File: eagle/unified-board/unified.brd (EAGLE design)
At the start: 203.2 x 101.6 mm, 299 parts, among them IC101 THAT151x, IC201 THAT151x, IC301 THAT151x, IC401 THAT151x, J103 phantom, J104 eqout, J105 eqout, J203 phantom, J204 eqout, J205 eqout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

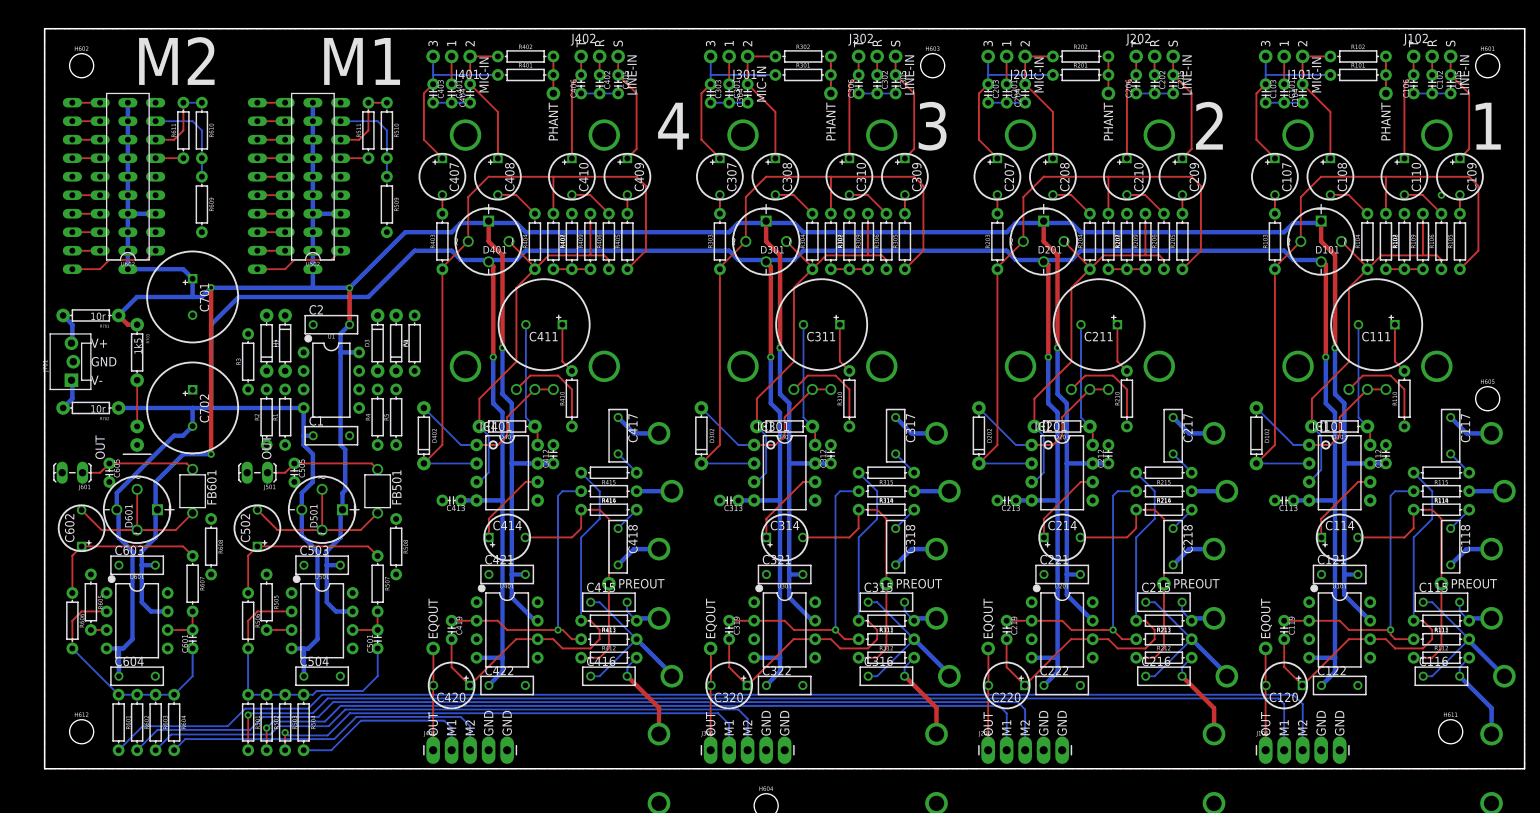
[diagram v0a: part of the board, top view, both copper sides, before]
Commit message: Possibly complete?
doublechecked all IC footprints.
Routed the peak detector & found 1uf caps for it.
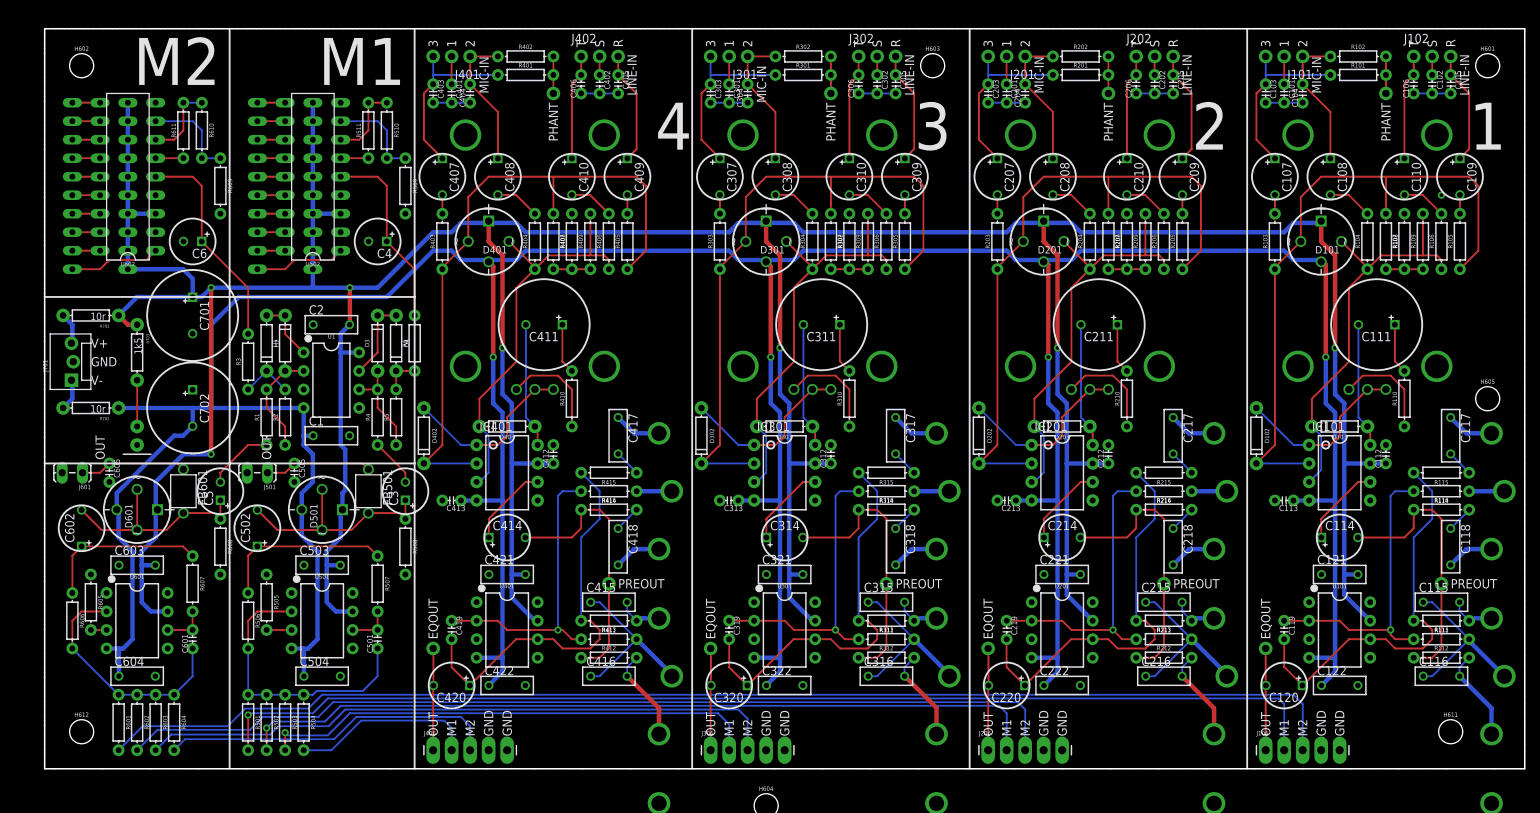
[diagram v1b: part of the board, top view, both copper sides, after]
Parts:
- added C3, C4, C5, C6: 1uf/160V, mixer:CAP-PANA-2.5LS-6DIAM
- moved R509 3.59 mm to (49.5, 80.0)
- moved R609 3.59 mm to (24.1, 80.0)
- moved R1 2.54 mm to (30.5, 48.3)
- moved R2 2.54 mm to (33.0, 48.3)
- moved C701 2.54 mm to (20.3, 62.2)
- moved R508 1.27 mm to (49.5, 30.5)
- moved FB601 1.27 mm to (19.1, 38.1)
- moved R608 1.27 mm to (24.1, 30.5)
- moved FB501 1.27 mm to (44.5, 38.1)
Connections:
- new net N$38: C3.NEG, R4.P$1
- new net N$39: C4.POS, R6.P$2, U502.5
- new net N$54: C5.NEG, R1.P$1
- net GND: now also C4.NEG, C6.NEG
- net N$11: now also C5.POS; no longer R1.P$1
- net N$152: now also C3.POS; no longer U502.5
- net N$23: now also C6.POS
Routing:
- net N$23: track 0.00 -> 29.8 mm
- net N$39: track 0.00 -> 26.2 mm
- net N$5: track 0.00 -> 14.8 mm
- net N$25: track 0.00 -> 13.8 mm
- net N$26: track 0.00 -> 11.2 mm
- net N$54: track 0.00 -> 9.22 mm
- net N$9: track 0.00 -> 8.67 mm
- net N$18: track 0.00 -> 7.18 mm
- net N$152: track 24.2 -> 30.9 mm
- net N$11: track 22.9 -> 29.6 mm
- net N$38: track 0.00 -> 6.68 mm
- net N$36: track 0.00 -> 5.08 mm
- net N$46: track 0.00 -> 3.81 mm
- net N$7: track 16.0 -> 14.7 mm
- net N$151: track 16.0 -> 14.7 mm

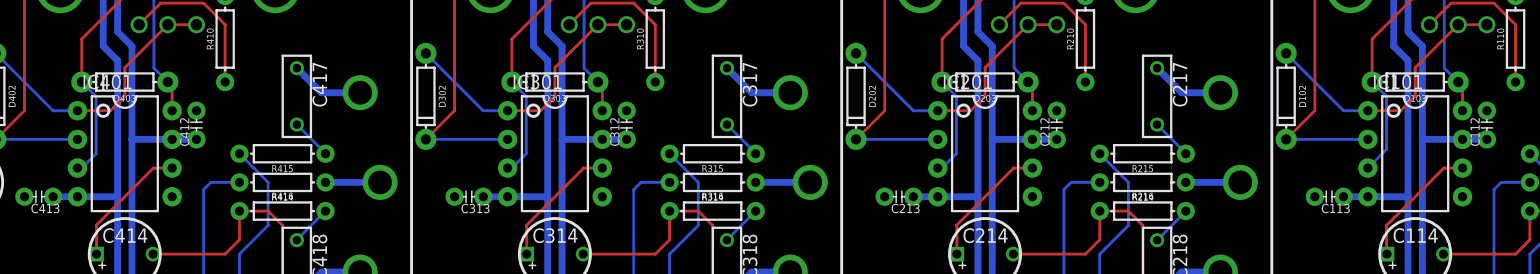
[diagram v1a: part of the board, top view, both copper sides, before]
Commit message: More touchups.
Doublechecked rotary switch direction and values.
Added some dimension lines.
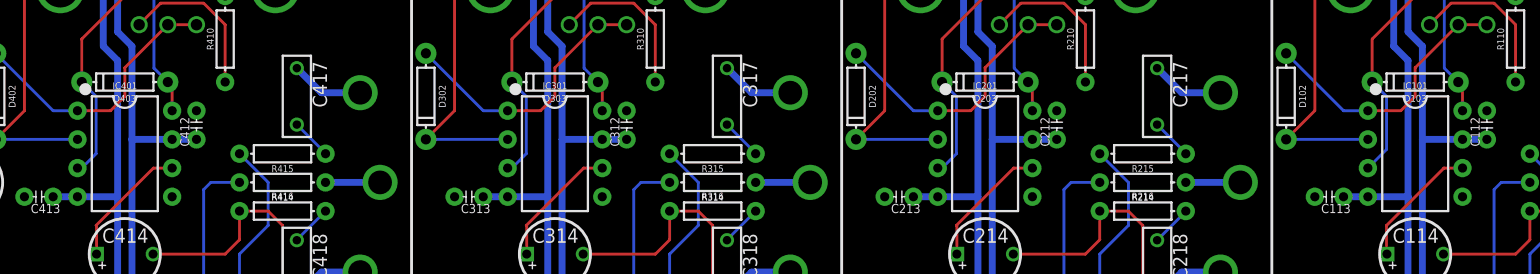
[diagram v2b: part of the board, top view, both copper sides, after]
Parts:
- IC101, IC201, IC301, IC401: value THAT151x -> THAT1512; device mosfet:DIP08-KIT -> mixer:DIP08-KIT
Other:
- board text added: "16x ??"
- board text added: "4x 10mm??"
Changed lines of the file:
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@@
 <layer number="19" name="Unrouted" color="6" fill="1" visible="yes" active="yes"/>
 <layer number="20" name="Dimension" color="15" fill="1" visible="yes" active="yes"/>
-<layer number="21" name="tPlace" color="16" fill="1" visible="yes" active="yes"/>
-<layer number="22" name="bPlace" color="14" fill="1" visible="no" active="yes"/>
+<layer number="21" name="tPlace" color="16" fill="1" visible="no" active="yes"/>
+<layer number="22" name="bPlace" color="14" fill="1" visible="yes" active="yes"/>
 <layer number="23" name="tOrigins" color="15" fill="1" visible="yes" active="yes"/>
-<layer number="24" name="bOrigins" color="15" fill="1" visible="no" active="yes"/>
+<layer number="24" name="bOrigins" color="15" fill="1" visible="yes" active="yes"/>
 <layer number="25" name="tNames" color="7" fill="1" visible="yes" active="yes"/>
 <layer number="26" name="bNames" color="7" fill="1" visible="no" active="yes"/>
@@
 <layer number="45" name="Holes" color="7" fill="1" visible="no" active="yes"/>
 <layer number="46" name="Milling" color="3" fill="1" visible="no" active="yes"/>
-<layer number="47" name="Measures" color="7" fill="1" visible="no" active="yes"/>
+<layer number="47" name="Measures" color="7" fill="1" visible="yes" active="yes"/>
 <layer number="48" name="Document" color="7" fill="1" visible="no" active="yes"/>
 <layer number="49" name="Reference" color="7" fill="1" visible="no" active="yes"/>
@@
 <wire x1="0" y1="101.6" x2="0" y2="0" width="0.2032" layer="20"/>
 <wire x1="-2.54" y1="68" x2="-2.54" y2="0" width="0.254" layer="51"/>
-<wire x1="25.4" y1="103.5" x2="25.4" y2="-0.06" width="0.254" layer="51"/>
+<wire x1="25.4" y1="100.96" x2="25.4" y2="-0.06" width="0.254" layer="51"/>
 <wire x1="-12.7" y1="102.23" x2="-12.7" y2="-54.67" width="0.254" layer="51"/>
-<wire x1="88.9" y1="103.5" x2="88.9" y2="-0.06" width="0.254" layer="51"/>
-<wire x1="50.8" y1="103.5" x2="50.8" y2="-0.06" width="0.254" layer="51"/>
-<wire x1="165.1" y1="103.5" x2="165.1" y2="-0.06" width="0.254" layer="51"/>
-<wire x1="127" y1="103.5" x2="127" y2="-0.06" width="0.254" layer="51"/>
+<wire x1="88.9" y1="100.96" x2="88.9" y2="-0.06" width="0.254" layer="51"/>
+<wire x1="50.8" y1="100.96" x2="50.8" y2="-0.06" width="0.254" layer="51"/>
+<wire x1="165.1" y1="100.96" x2="165.1" y2="-0.06" width="0.254" layer="51"/>
+<wire x1="127" y1="100.96" x2="127" y2="-0.06" width="0.254" layer="51"/>
 <wire x1="0.64" y1="-25.4" x2="203.26" y2="-25.4" width="0.254" layer="51"/>
 <wire x1="0.64" y1="-50.8" x2="203.26" y2="-50.8" width="0.254" layer="51"/>
@@
 <wire x1="0" y1="41.91" x2="50.8" y2="41.91" width="0.254" layer="21"/>
 <wire x1="0" y1="64.77" x2="50.8" y2="64.77" width="0.254" layer="21"/>
-<wire x1="165.1" y1="101.6" x2="165.1" y2="0" width="0.254" layer="22"/>
+<wire x1="181.61" y1="101.6" x2="181.61" y2="-50.8" width="0.254" layer="22"/>
 <wire x1="127" y1="101.6" x2="127" y2="0" width="0.254" layer="22"/>
 <wire x1="88.9" y1="101.6" x2="88.9" y2="0" width="0.254" layer="22"/>
@@
 <wire x1="50.8" y1="41.91" x2="0" y2="41.91" width="0.254" layer="22"/>
 <wire x1="50.8" y1="64.77" x2="0" y2="64.77" width="0.254" layer="22"/>
+<wire x1="143.51" y1="101.6" x2="143.51" y2="-52.07" width="0.254" layer="22"/>
+<wire x1="105.41" y1="101.6" x2="105.41" y2="-50.8" width="0.254" layer="22"/>
+<wire x1="67.31" y1="101.6" x2="67.31" y2="71.12" width="0.254" layer="22"/>
+<wire x1="67.31" y1="71.12" x2="67.31" y2="38.1" width="0.254" layer="22"/>
+<wire x1="67.31" y1="38.1" x2="67.31" y2="12.7" width="0.254" layer="22"/>
+<wire x1="67.31" y1="12.7" x2="67.31" y2="-50.8" width="0.254" layer="22"/>
+<wire x1="67.31" y1="71.12" x2="203.2" y2="71.12" width="0.254" layer="22"/>
+<wire x1="67.31" y1="38.1" x2="203.2" y2="38.1" width="0.254" layer="22"/>
+<wire x1="67.31" y1="12.7" x2="203.2" y2="12.7" width="0.254" layer="22"/>
+<wire x1="67.31" y1="-12.7" x2="203.2" y2="-12.7" width="0.254" layer="22"/>
+<wire x1="67.31" y1="-38.1" x2="203.2" y2="-38.1" width="0.254" layer="22"/>
+<dimension x1="0" y1="101.6" x2="203.2" y2="101.6" x3="101.6" y3="130.81" textsize="1.778" textratio="15" layer="47" unit="inch"/>
+<dimension x1="203.2" y1="101.6" x2="181.61" y2="101.6" x3="192.405" y3="105.41" textsize="1.778" textratio="15" layer="47" unit="inch"/>
+<dimension x1="203.2" y1="101.6" x2="143.51" y2="101.6" x3="173.355" y3="109.22" textsize="1.778" textratio="15" layer="47" unit="inch"/>
+<dimension x1="203.2" y1="101.6" x2="105.41" y2="101.6" x3="154.305" y3="114.3" textsize="1.778" textratio="15" layer="47" unit="inch"/>
+<dimension x1="203.2" y1="101.6" x2="67.31" y2="101.6" x3="135.255" y3="118.11" textsize="1.778" textratio="15" layer="47" unit="inch"/>
+<dimension x1="203.2" y1="101.6" x2="203.2" y2="0" x3="236.22" y3="50.8" textsize="1.778" textratio="15" layer="47" unit="inch"/>
+<dimension x1="203.2" y1="0" x2="203.2" y2="-50.8" x3="236.22" y3="-25.4" textsize="1.778" textratio="15" layer="47" unit="inch"/>
+<dimension x1="203.2" y1="101.6" x2="203.2" y2="71.12" x3="208.28" y3="86.36" textsize="1.778" textratio="15" layer="47" unit="inch"/>
+<dimension x1="203.2" y1="101.6" x2="203.2" y2="38.1" x3="213.36" y3="69.85" textsize="1.778" textratio="15" layer="47" unit="inch"/>
+<dimension x1="203.2" y1="101.6" x2="203.2" y2="12.7" x3="218.44" y3="57.15" textsize="1.778" textratio="15" layer="47" unit="inch"/>
+<dimension x1="203.2" y1="101.6" x2="203.2" y2="-12.7" x3="224.79" y3="44.45" textsize="1.778" textratio="15" layer="47" unit="inch"/>
+<dimension x1="203.2" y1="101.6" x2="203.2" y2="-38.1" x3="229.87" y3="31.75" textsize="1.778" textratio="15" layer="47" unit="inch"/>
+<dimension x1="181.61" y1="71.12" x2="241.3" y2="87.63" x3="252.73" y3="87.63" textsize="1.778" textratio="15" layer="47" dtype="leader" unit="inch"/>
+<dimension x1="181.61" y1="38.1" x2="243.84" y2="62.23" x3="252.73" y3="62.23" textsize="1.778" textratio="15" layer="47" dtype="leader" unit="inch"/>
+<text x="252.73" y="87.63" size="1.778" layer="47" font="vector" ratio="15">4x 10mm??</text>
+<text x="252.73" y="62.23" size="1.778" layer="47" font="vector" ratio="15">16x ??</text>
 </plain>
 <attributes>
@@
 <attribute name="MOUSER" value="505-MKS2.1/63/5" x="191.77" y="12.7" size="1.778" layer="27" display="off"/>
 </element>
-<element name="IC101" library="mosfet" package="DIP08-KIT" value="THAT151x" x="177.8" y="40.64" rot="R270"/>
+<element name="IC101" library="mixer" package="DIP08-KIT" value="THAT1512" x="177.8" y="40.64" rot="R270">
+<attribute name="MOUSER" value="887-1512P08-U " x="177.8" y="40.64" size="1.778" layer="27" rot="R270" display="off"/>
+</element>
 <element name="D103" library="SparkFun-DiscreteSemi" package="DIODE-1N4148" value="200mA/100V/1V" x="177.8" y="46.99" rot="R180">
 <attribute name="PROD_ID" value="DIO-08378" x="177.8" y="46.99" size="1.778" layer="27" font="vector" ratio="15" rot="R180" display="off"/>
@@
 <attribute name="MOUSER" value="505-MKS2.1/63/5" x="-88.9" y="27.94" size="1.778" layer="27" font="vector" ratio="15" display="off"/>
 </element>
-<element name="IC201" library="mosfet" package="DIP08-KIT" value="THAT151x" x="139.7" y="40.64" rot="R270"/>
+<element name="IC201" library="mixer" package="DIP08-KIT" value="THAT1512" x="139.7" y="40.64" rot="R270">
+<attribute name="MOUSER" value="887-1512P08-U " x="139.7" y="40.64" size="1.778" layer="27" rot="R270" display="off"/>
+</element>
 <element name="D203" library="SparkFun-DiscreteSemi" package="DIODE-1N4148" value="200mA/100V/1V" x="139.7" y="46.99" rot="R180">
 <attribute name="PROD_ID" value="DIO-08378" x="289.56" y="138.43" size="1.778" layer="27" font="vector" ratio="15" rot="R180" display="off"/>
@@
 <attribute name="MOUSER" value="505-MKS2.1/63/5" x="-127" y="27.94" size="1.778" layer="27" font="vector" ratio="15" display="off"/>
 </element>
-<element name="IC301" library="mosfet" package="DIP08-KIT" value="THAT151x" x="101.6" y="40.64" rot="R270"/>
+<element name="IC301" library="mixer" package="DIP08-KIT" value="THAT1512" x="101.6" y="40.64" rot="R270">
+<attribute name="MOUSER" value="887-1512P08-U " x="101.6" y="40.64" size="1.778" layer="27" rot="R270" display="off"/>
+</element>
 <element name="D303" library="SparkFun-DiscreteSemi" package="DIODE-1N4148" value="200mA/100V/1V" x="101.6" y="46.99" rot="R180">
 <attribute name="PROD_ID" value="DIO-08378" x="251.46" y="138.43" size="1.778" layer="27" font="vector" ratio="15" rot="R180" display="off"/>
@@
 <attribute name="MOUSER" value="505-MKS2.1/63/5" x="-165.1" y="27.94" size="1.778" layer="27" font="vector" ratio="15" display="off"/>
 </element>
-<element name="IC401" library="mosfet" package="DIP08-KIT" value="THAT151x" x="63.5" y="40.64" rot="R270"/>
+<element name="IC401" library="mixer" package="DIP08-KIT" value="THAT1512" x="63.5" y="40.64" rot="R270">
+<attribute name="MOUSER" value="887-1512P08-U " x="63.5" y="40.64" size="1.778" layer="27" rot="R270" display="off"/>
+</element>
 <element name="D403" library="SparkFun-DiscreteSemi" package="DIODE-1N4148" value="200mA/100V/1V" x="63.5" y="46.99" rot="R180">
 <attribute name="PROD_ID" value="DIO-08378" x="213.36" y="138.43" size="1.778" layer="27" font="vector" ratio="15" rot="R180" display="off"/>
